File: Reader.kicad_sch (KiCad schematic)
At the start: 41 parts, among them J1 Conn_01x04, J2 Amphenol Dubox ‎76383-402LF‎, J3 Conn_01x04, J4 Conn_01x08, J5 Conn_01x10, J6 Conn_01x03, J7 Conn_01x02, Q1 2N7002, Q2 2N7002, Q3 2N7002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

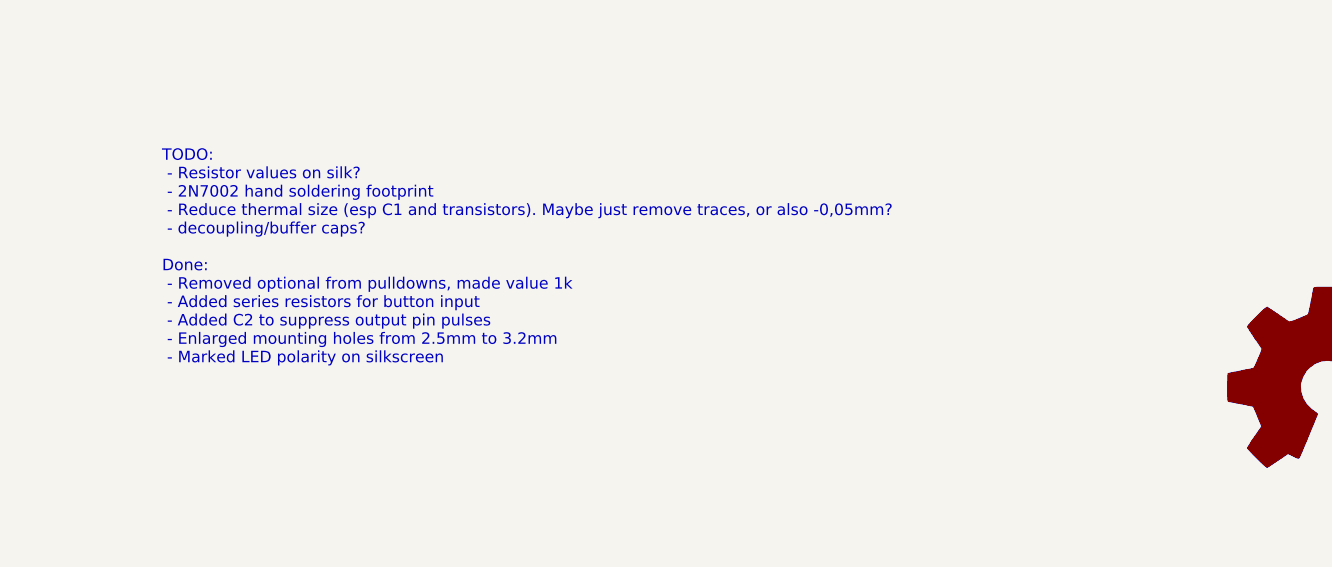
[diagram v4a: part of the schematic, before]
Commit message: Reduce overly wide thermal reliefs due to wide GND traces
The thermal relief spoke width was 0,3mm, but there were also explicit
GND traces of 0,5mm that made some components (esp C1 and some
transistors) hard to solder. This reduces the trace width to 0,3mm,
hopefully alleviating this issue.
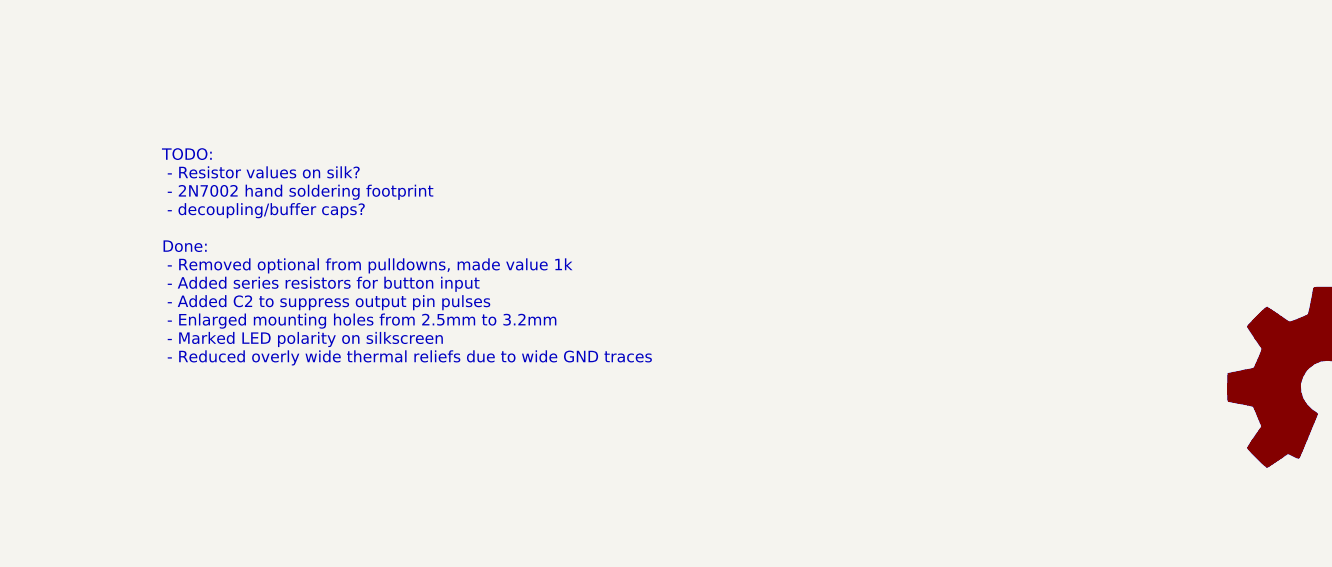
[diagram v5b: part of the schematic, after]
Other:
- note added: "TODO: - Resistor values on silk? - 2N7002 hand soldering footprint - decoupling/buffer caps? Done: - Removed optional from pulldowns, made value 1k - Added series resistors for button input - Added C2 to suppress output pin pulses - Enlarged mounting holes from 2.5mm to 3.2mm - Marked LED polarity on silkscreen - Reduced overly wide thermal reliefs due to wide GND traces"
- note removed: "TODO: - Resistor values on silk? - 2N7002 hand soldering footprint - Reduce thermal size (esp C1 and transistors). Maybe just remove traces, or also -0,05mm? - decoupling/buffer caps? Done: - Removed optional from pulldowns, made value 1k - Added series resistors for button input - Added C2 to suppress output pin pulses - Enlarged mounting holes from 2.5mm to 3.2mm - Marked LED polarity on silksc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"
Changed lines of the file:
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@@
     (stroke (width 0) (type default))
   )
-  (text "TODO:\n - Resistor values on silk?\n - 2N7002 hand soldering footprint\n - Reduce thermal size (esp C1 and transistors). Maybe just remove traces, or also -0,05mm?\n - decoupling/buffer caps?\n\nDone:\n - Removed optional from pulldowns, made value 1k\n - Added series resistors for button input\n - Added C2 to suppress output pin pulses\n - Enlarged mounting holes from 2.5mm to 3.2mm\n - Marked LED polarity on silkscreen\n"
+  (text "TODO:\n - Resistor values on silk?\n - 2N7002 hand soldering footprint\n - decoupling/buffer caps?\n\nDone:\n - Removed optional from pulldowns, made value 1k\n - Added series resistors for button input\n - Added C2 to suppress output pin pulses\n - Enlarged mounting holes from 2.5mm to 3.2mm\n - Marked LED polarity on silkscreen\n - Reduced overly wide thermal reliefs due to wide GND traces"
     (at 116.84 152.4 0)
     (effects (font (size 1.27 1.27)) (justify left bottom))

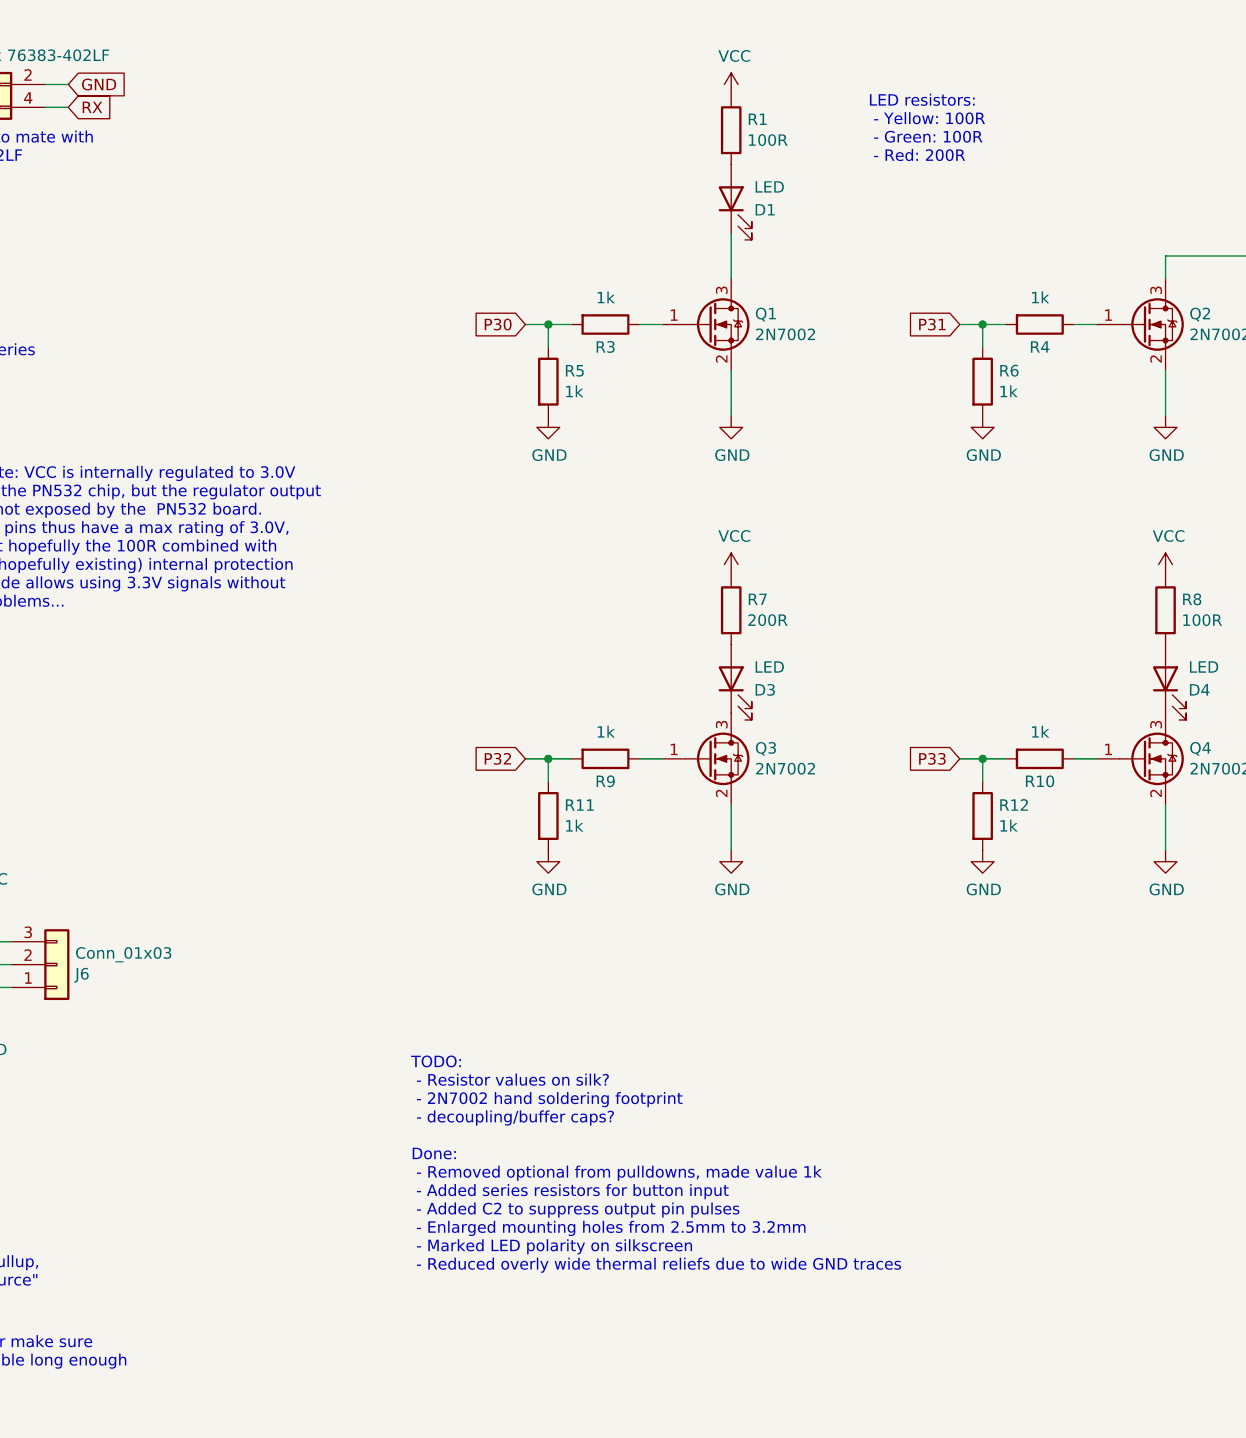
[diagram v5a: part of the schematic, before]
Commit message: Add input supply buffer cap
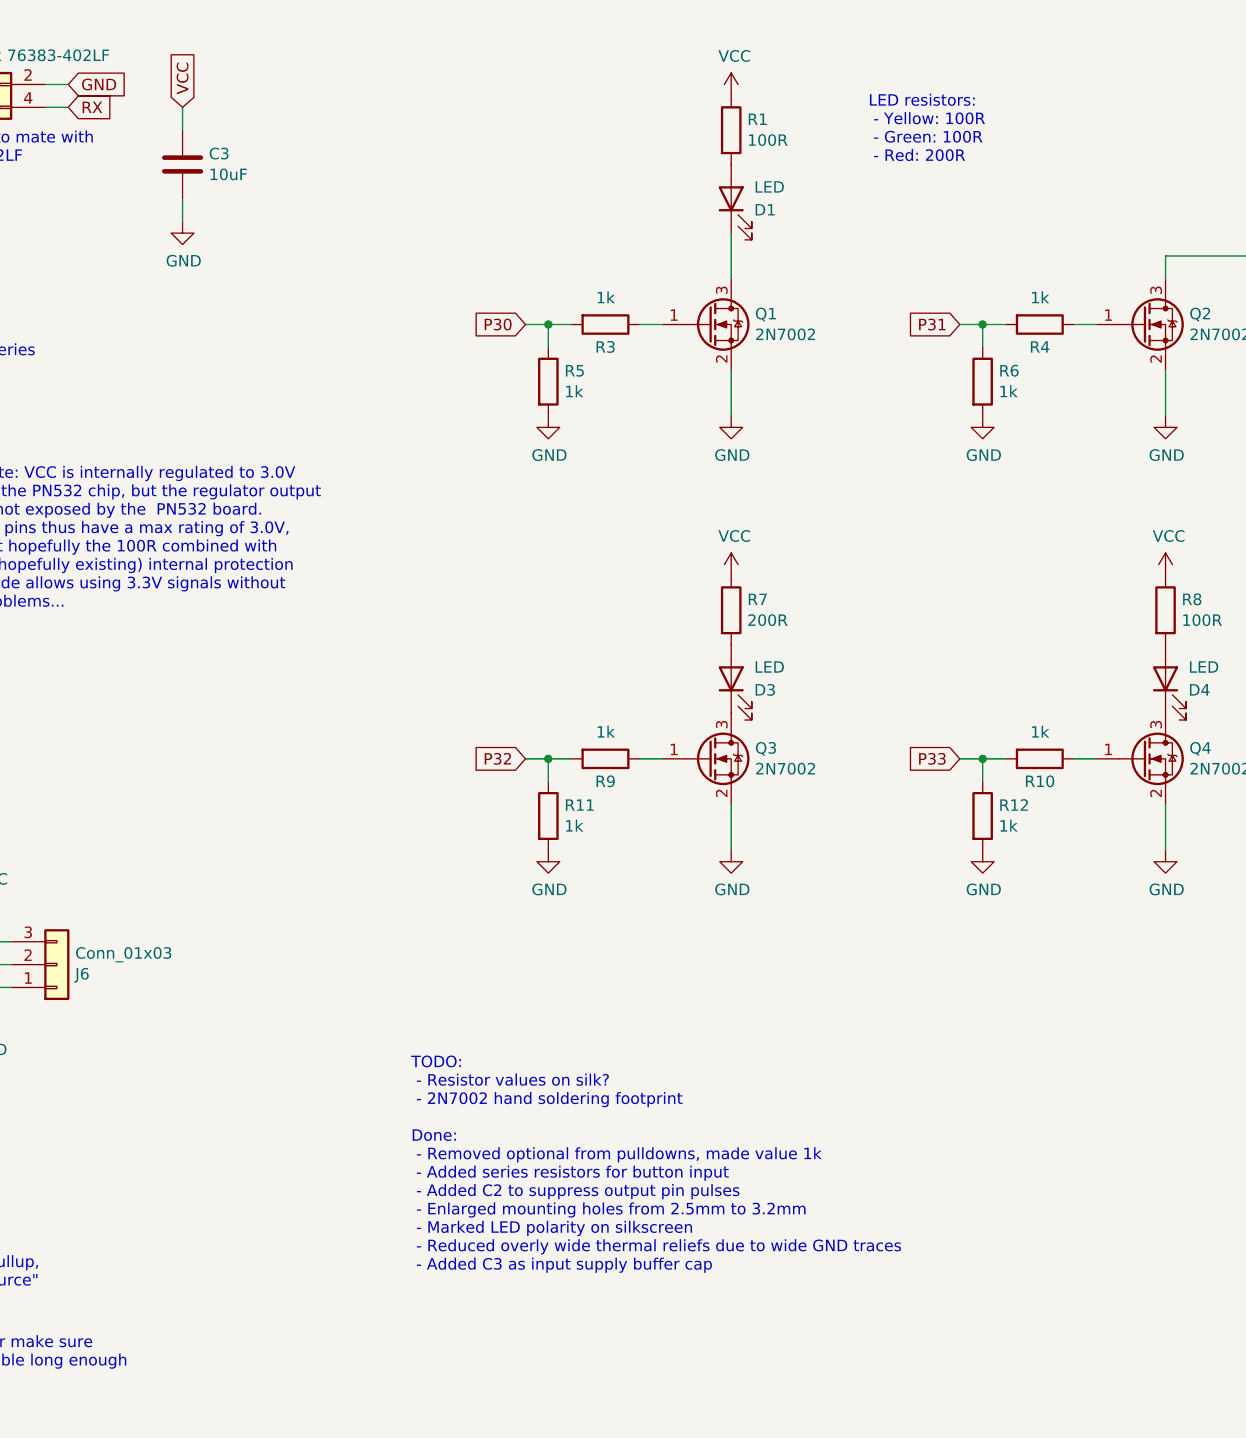
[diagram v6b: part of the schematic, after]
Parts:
- added C3: 10uF, Capacitor_SMD:C_0805_2012Metric_Pad1.18x1.45mm_HandSolder, symbol Device:C
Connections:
- net GND: now also C3.2
- net VCC: now also C3.1
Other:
- note added: "TODO: - Resistor values on silk? - 2N7002 hand soldering footprint Done: - Removed optional from pulldowns, made value 1k - Added series resistors for button input - Added C2 to suppress output pin pulses - Enlarged mounting holes from 2.5mm to 3.2mm - Marked LED polarity on silkscreen - Reduced overly wide thermal reliefs due to wide GND traces - Added C3 as input supply buffer cap"
- note removed: "TODO: - Resistor values on silk? - 2N7002 hand soldering footprint - decoupling/buffer caps? Done: - Removed optional from pulldowns, made value 1k - Added series resistors for button input - Added C2 to suppress output pin pulses - Enlarged mounting holes from 2.5mm to 3.2mm - Marked LED polarity on silkscreen - Reduced overly wide thermal reliefs due to wide GND traces"
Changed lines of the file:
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@@
+    (stroke (width 0) (type default))
+  )
+  (wire (pts (xy 91.44 33.02) (xy 91.44 35.56))
     (stroke (width 0) (type default))
   )
@@
     (stroke (width 0) (type default))
   )
+  (wire (pts (xy 91.44 22.86) (xy 91.44 25.4))
+    (stroke (width 0) (type default))
+  )
   (wire (pts (xy 69.85 123.19) (xy 69.85 120.65))
     (stroke (width 0) (type default))
@@
     (stroke (width 0) (type default))
   )
-  (text "TODO:\n - Resistor values on silk?\n - 2N7002 hand soldering footprint\n - decoupling/buffer caps?\n\nDone:\n - Removed optional from pulldowns, made value 1k\n - Added series resistors for button input\n - Added C2 to suppress output pin pulses\n - Enlarged mounting holes from 2.5mm to 3.2mm\n - Marked LED polarity on silkscreen\n - Reduced overly wide thermal reliefs due to wide GND traces"
+  (text "TODO:\n - Resistor values on silk?\n - 2N7002 hand soldering footprint\n\nDone:\n - Removed optional from pulldowns, made value 1k\n - Added series resistors for button input\n - Added C2 to suppress output pin pulses\n - Enlarged mounting holes from 2.5mm to 3.2mm\n - Marked LED polarity on silkscreen\n - Reduced overly wide thermal reliefs due to wide GND traces\n - Added C3 as input supply buffer cap"
     (at 116.84 152.4 0)
     (effects (font (size 1.27 1.27)) (justify left bottom))
@@
     (property "Intersheetrefs" "${INTERSHEET_REFS}" (at 28.3494 52.07 0)
       (effects (font (size 1.27 1.27)) (justify right) hide)
+    )
+  )
+  (global_label "VCC" (shape input) (at 91.44 22.86 90) (fields_autoplaced)
+    (effects (font (size 1.27 1.27)) (justify left))
+    (property "Intersheetrefs" "${INTERSHEET_REFS}" (at 91.44 16.9004 90)
+      (effects (font (size 1.27 1.27)) (justify left) hide)
     )
   )
@@
         )
       )
+    )
+  )
+  (symbol (lib_id "Device:C") (at 91.44 29.21 0) (unit 1)
+    (in_bom yes) (on_board yes) (dnp no)
+    (property "Reference" "C3" (at 94.361 28.0416 0)
+      (effects (font (size 1.27 1.27)) (justify left))
+    )
+    (property "Value" "10uF" (at 94.361 30.353 0)
+      (effects (font (size 1.27 1.27)) (justify left))
+    )
+    (property "Footprint" "Capacitor_SMD:C_0805_2012Metric_Pad1.18x1.45mm_HandSolder" (at 92.4052 33.02 0)
+      (effects (font (size 1.27 1.27)) hide)
+    )
+    (property "Datasheet" "~" (at 91.44 29.21 0)
+      (effects (font (size 1.27 1.27)) hide)
+    )
+    (pin "1")
+    (pin "2")
+    (instances
+      (project "Reader"
+        (path "/f5709391-a389-450b-a647-2f06b3cb0d95"
+          (reference "C3") (unit 1)
+        )
+      )
+    )
+  )
+  (symbol (lib_id "power:GND") (at 91.44 35.56 0) (unit 1)
+    (in_bom yes) (on_board yes) (dnp no)
+    (property "Reference" "#PWR019" (at 91.44 41.91 0)
+      (effects (font (size 1.27 1.27)) hide)
+    )
+    (property "Value" "GND" (at 91.567 39.9542 0)
+      (effects (font (size 1.27 1.27)))
+    )
+    (property "Footprint" "" (at 91.44 35.56 0)
+      (effects (font (size 1.27 1.27)) hide)
+    )
+    (property "Datasheet" "" (at 91.44 35.56 0)
+      (effects (font (size 1.27 1.27)) hide)
+    )
+    (pin "1")
+    (instances
+      (project "Reader"
+        (path "/f5709391-a389-450b-a647-2f06b3cb0d95"
+          (reference "#PWR019") (unit 1)
+        )
+      )
